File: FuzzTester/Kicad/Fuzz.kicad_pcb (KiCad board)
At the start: 2 copper layers, 100 x 82 mm, 142 parts, among them J1 Audio In/Out JST XH, J10 Key Pad JST XH, J11 LCD JST XH, J12 Bypass Switch JST XH, J2 POT B10K JST XH, J3 POT B5K JST XH, J4 VOL POT A100K JST XH, J5 PowerTest_PinHeader, J6 9V Power JST XH, J7 Boot Reset PinHeader, J8 SPI Test PinHeader, J9 SWD_PinHeader, Q1 PN2222A, Q10 2SC1815, Q11 S8050, Q12 S9013, Q13 S9014, Q14 S9018, Q15 BC848B, Q16 2SC1623, Q17 MPSA18, Q18 MPSA18, Q19 2N5088, Q2 MMBT3904, Q20 2N5088, Q21 PN2222A, Q22 MMBT3904, Q23 MMBT5551L, Q24 MMBTA42, Q25 BC807, Q26 BC846, Q27 BC847B, Q28 BC847C, Q29 C945, Q3 MMBT5551L, Q30 2SC1815, Q31 S8050, Q32 S9013, Q33 S9014, Q34 S9018, Q35 BC848B, Q36 2SC1623, Q37 MPSA18, Q38 MPSA18, Q39 2N5088, Q4 MMBTA42, Q40 2N5088, Q5 BC807, Q6 BC846, Q7 BC847B, Q8 BC847C, Q9 C945, U1 AMS1117-5.0, U10 CD4052B, U11 CD4052B, U12 CD4052B, U13 CD4052B, U14 CD4051B, U15 CD4052B, U16 CD4051B, U17 CD4052B, U18 CD4052B, U19 CD4052B, U2 AMS1117-3.3, U20 74HC595, U21 CD4051B, U22 4504, U23 4504, U24 4504, U25 CD4053B, U3 STM32F103C8Tx, U4 CD4051B, U5 74HC595, U6 CD4052B, U7 CD4051B, U8 CD4052B, U9 CD4051B, Y1 8MHz

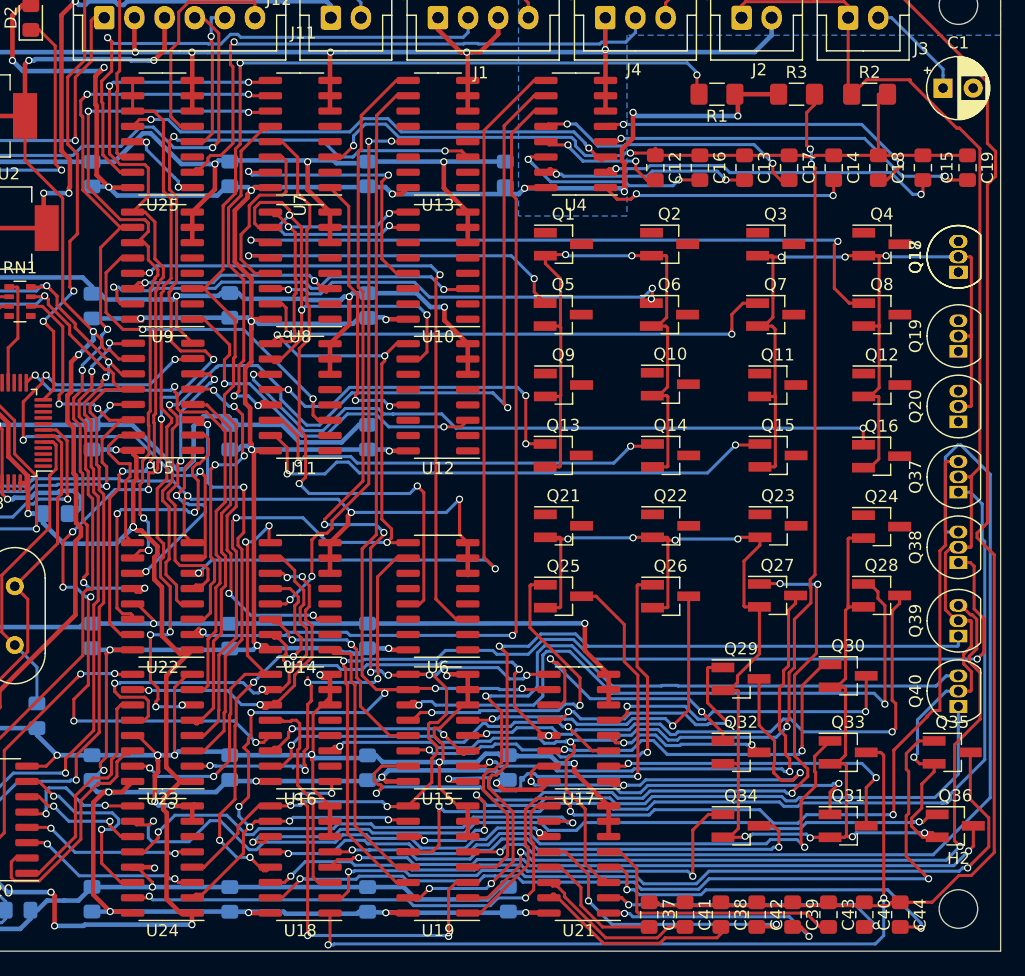
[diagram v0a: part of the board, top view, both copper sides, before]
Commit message: Routing finished, todo: AGND
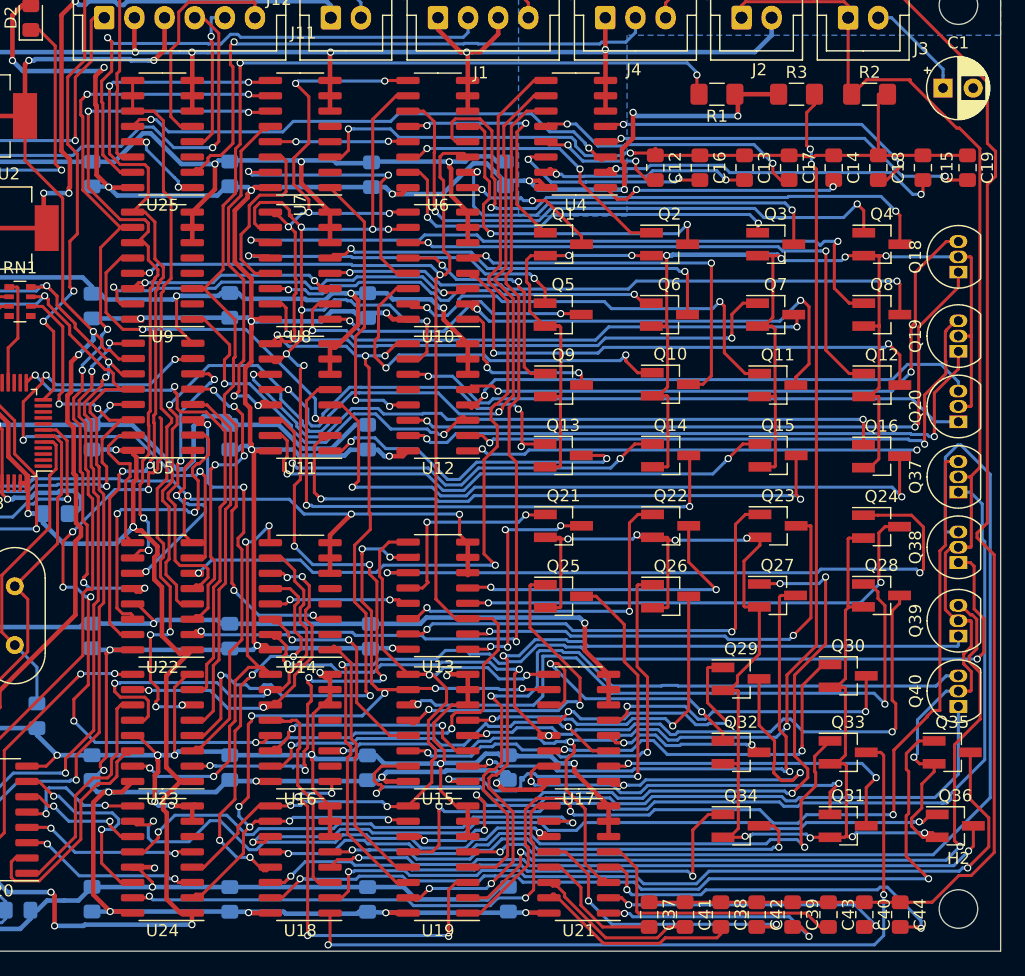
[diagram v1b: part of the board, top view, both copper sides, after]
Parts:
- removed Q17: MPSA18, Package_TO_SOT_THT:TO-92_Inline
- moved C28 38.4 mm to (77.7, 85.9)
- moved U6 38.4 mm to (83.3, 44.2)
- moved U13 38.3 mm to (83.3, 82.5)
- moved C21 38.3 mm to (77.8, 47.6)
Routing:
- net /TransistorsB/16_COLLECTOR: track 0.00 -> 58.6 mm, vias 0 -> 2
- net /TransistorsB/18_BASE: track 0.00 -> 56.6 mm, vias 0 -> 2
- net /TransistorsC/4_BASE: track 0.00 -> 55.5 mm, vias 0 -> 2
- net /TransistorsB/19_BASE: track 0.00 -> 52.3 mm, vias 0 -> 2
- net /TransistorsB/8_COLLECTOR: track 0.00 -> 50.9 mm, vias 0 -> 2
- net /TransistorsB/18_COLLECTOR: track 0.00 -> 50.8 mm, vias 0 -> 2
- net /TransistorsB/4_COLLECTOR: track 0.00 -> 50.6 mm, vias 0 -> 2
- net /TransistorsB/15_COLLECTOR: track 0.00 -> 50.3 mm, vias 0 -> 2
- net /TransistorsB/19_COLLECTOR: track 0.00 -> 50.0 mm, vias 0 -> 2
- net /TransistorsB/4_BASE: track 0.00 -> 49.2 mm, vias 0 -> 2
- net /TRANSISTOR_C_SELECTION_1: track 110.1 -> 62.3 mm, vias 8 -> 4
- net /TransistorsB/20_BASE: track 0.00 -> 47.8 mm, vias 0 -> 1
- net /TransistorsB/14_COLLECTOR: track 0.00 -> 47.3 mm, vias 0 -> 2
- net /TransistorsB/12_BASE: track 0.00 -> 47.1 mm, vias 0 -> 2
- net /TransistorsB/7_COLLECTOR: track 0.00 -> 45.5 mm, vias 0 -> 2
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
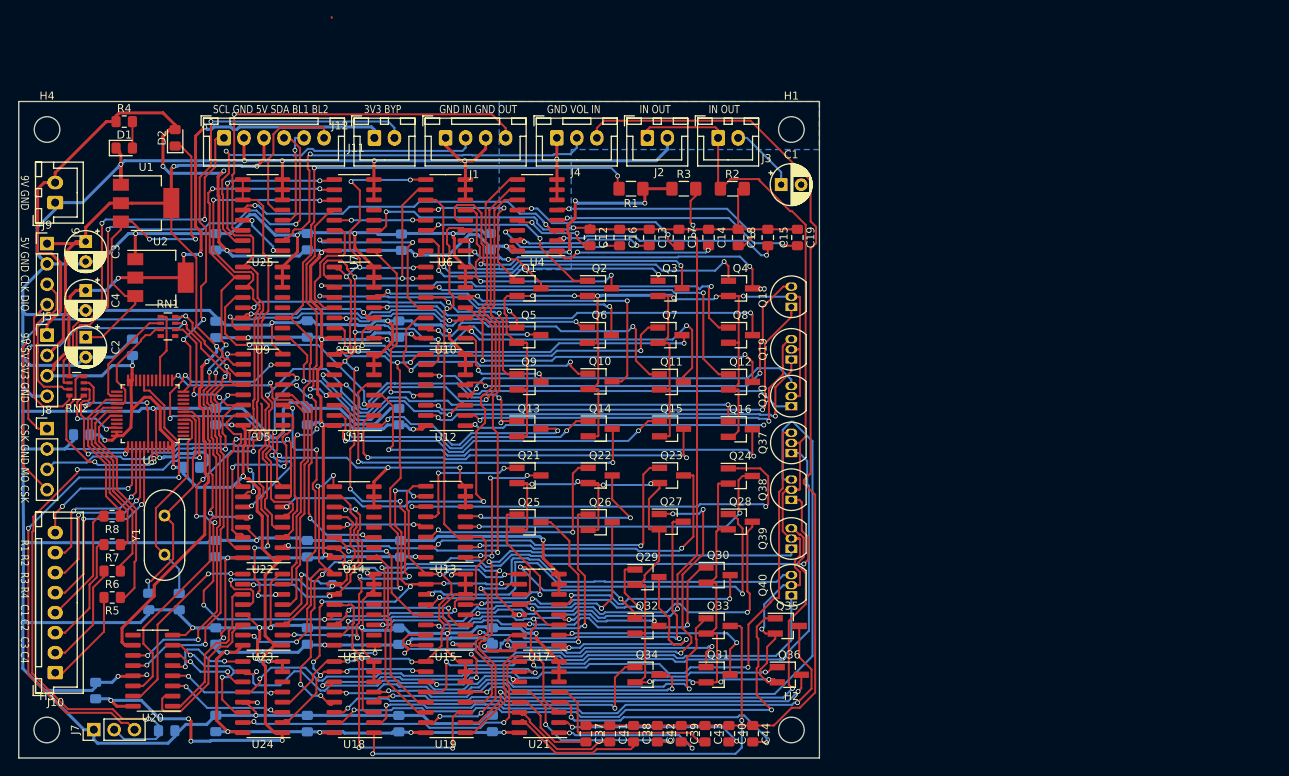
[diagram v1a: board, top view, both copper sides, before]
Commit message: GNDA, PCB DRC fixed
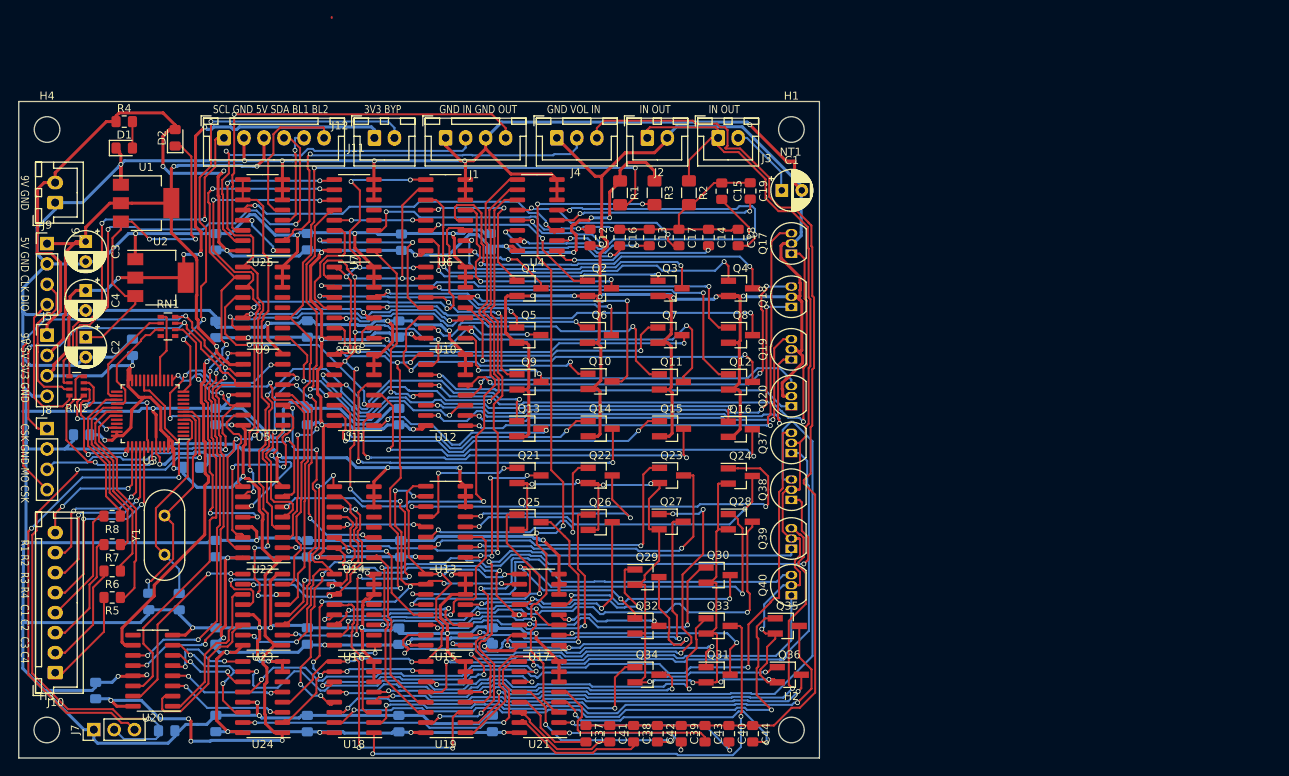
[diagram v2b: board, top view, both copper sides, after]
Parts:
- added NT1: Net-Tie_2, NetTie:NetTie-2_SMD_Pad0.5mm, F.Cu at (126.4, 37.5)
- added Q17: MPSA18, Package_TO_SOT_THT:TO-92_Inline, F.Cu at (126.5, 49.0)
- moved C19 8.28 mm to (121.4, 41.2)
- moved C15 8.16 mm to (117.8, 41.2)
- moved R2 5.45 mm to (113.7, 41.4), turned to 270 degrees
- moved R3 3.70 mm to (109.4, 41.4), turned to 270 degrees
- moved R1 1.46 mm to (105.1, 41.4), turned to 270 degrees
- moved C1 0.72 mm to (125.3, 41.1)
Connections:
- C1 pad 2: GND -> GNDA
- J2 pad 2: GND -> GNDA
- J4 pad 1: GND -> GNDA
- Q1 pad 2: GND -> GNDA
- Q10 pad 2: GND -> GNDA
- Q11 pad 2: GND -> GNDA
- Q12 pad 2: GND -> GNDA
- Q13 pad 2: GND -> GNDA
- Q14 pad 2: GND -> GNDA
- Q15 pad 2: GND -> GNDA
- Q16 pad 2: GND -> GNDA
- Q18 pad 2: GND -> GNDA
- Q19 pad 2: GND -> GNDA
- Q2 pad 2: GND -> GNDA
- Q20 pad 2: GND -> GNDA
- Q3 pad 2: GND -> GNDA
- Q4 pad 2: GND -> GNDA
- Q5 pad 2: GND -> GNDA
- Q6 pad 2: GND -> GNDA
- Q7 pad 2: GND -> GNDA
- Q8 pad 2: GND -> GNDA
- Q9 pad 2: GND -> GNDA
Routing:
- net GNDA: track 0.00 -> 225.1 mm, vias 0 -> 6
- net GND: track 952.1 -> 829.8 mm, vias 42 -> 35
- net /TransistorsB/17_BASE: track 0.00 -> 71.9 mm, vias 0 -> 2
- net /TransistorsC/TG_1_COLLECTOR: track 80.7 -> 32.6 mm, vias 7 -> 2
- net /TransistorsB/TG_1_COLLECTOR: track 69.8 -> 39.4 mm
- net /TransistorsB/17_COLLECTOR: track 37.7 -> 64.6 mm
- net /TransistorsC/BASE: track 97.1 -> 103.0 mm
- net Net-(C19-Pad2): track 31.6 -> 26.1 mm
- net /TransistorsC/EMITTER: track 219.2 -> 224.3 mm
- net /TransistorsB/19_BASE: track 52.3 -> 55.8 mm
- net /CAPACITOR_D_SELECTION_0: track 40.6 -> 44.0 mm
- net Net-(C18-Pad2): track 28.4 -> 31.4 mm
- net /TransistorsB/13_COLLECTOR: track 27.8 -> 24.9 mm
- net /TransistorsC/8_BASE: track 56.4 -> 59.2 mm
- net /TransistorsC/5_BASE: track 28.3 -> 31.0 mm
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- removed copper zone on B.Cu, net GND
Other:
- net class GNDA added: clearance 0.2, trace_width 0.381, via_dia 0.6, via_drill 0.4

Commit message: DRC OK
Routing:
- net GNDA: track 225.1 -> 213.6 mm, vias 6 -> 8
- added copper zone on B.Cu, net GND
- added copper zone on F.Cu, net GND
- added copper zone on B.Cu, net GNDA
- added copper zone on F.Cu, net GNDA

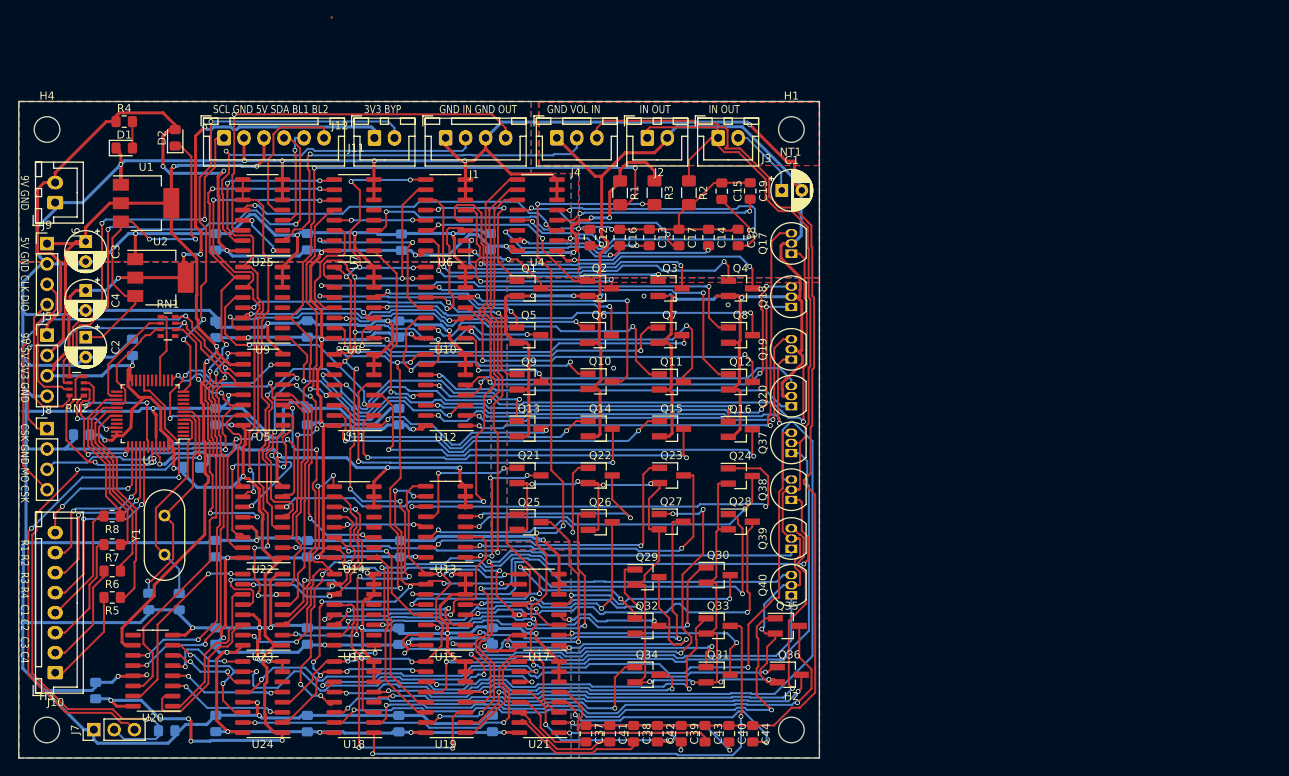
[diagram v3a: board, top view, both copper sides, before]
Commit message: Removed DRC errors, added logos
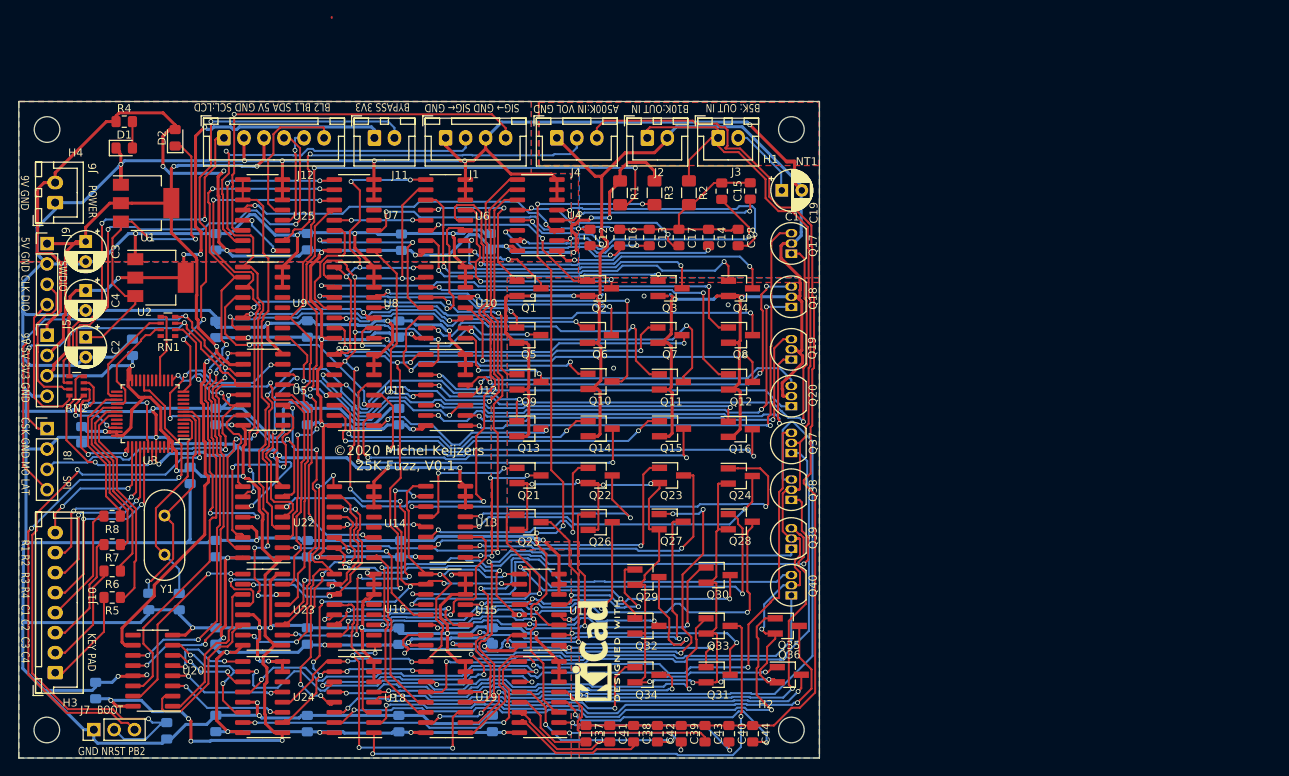
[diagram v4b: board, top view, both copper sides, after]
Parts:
- added REF**: KiCad-Logo2_20mm_SilkScreen, Symbol:KiCad-Logo2_20mm_SilkScreen, B.Cu at (107.2, 69.5)
- added REF**: KiCad-Logo2_5mm_SilkScreen, Symbol:KiCad-Logo2_5mm_SilkScreen, F.Cu at (102.1, 98.6)
- moved C9 1.02 mm to (51.4, 76.7), turned to 90 degrees
- turned C10 to 270 degrees
- turned C7 to 90 degrees
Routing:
- net GND: track 830.3 -> 833.3 mm, vias 35 -> 36
- net /Mcu/NRST: track 76.9 -> 78.5 mm
- net +3V3: track 206.2 -> 205.1 mm
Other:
- board text added: "25K Fuzz, V0.1"
- board text added: "A500K:IN VOL GND"
- board text added: "B10K:OUT IN"
- board text added: "B5K: OUT IN"
- board text added: "BL2 BL1 SDA 5V GND SCL:LCD"
- board text added: "BOOT"
- board text added: "BYPASS 3V3"
- board text added: "CSK GND MO LAT"
- board text added: "GND NRST PB2"
- board text added: "KEY PAD"
- board text added: "POWER"
- board text added: "SIG→ GND SIG← GND"
- board text added: "SPI"
- board text added: "SWDIO"
- board text added: "©2020 Michel Keijzers"
- board text removed: "3V3 BYP"
- board text removed: "CSK GND MO CSK"
- board text removed: "GND IN GND OUT"
- board text removed: "GND VOL IN"
- board text removed: "IN OUT"
- board text removed: "SCL GND 5V SDA BL1 BL2"

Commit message: Analysis microcap
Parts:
- added REF**: DIP-28_W15.24mm_LongPads, Package_DIP:DIP-28_W15.24mm_LongPads, F.Cu at (152.0, 91.1)
- added REF**: DIP-28_W15.24mm_LongPads, Package_DIP:DIP-28_W15.24mm_LongPads, F.Cu at (152.1, 51.6)
- added REF**: DIP-28_W15.24mm_LongPads, Package_DIP:DIP-28_W15.24mm_LongPads, F.Cu at (152.2, 71.9)
